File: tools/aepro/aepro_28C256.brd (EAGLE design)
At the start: 53 x 80 mm, 22 parts, among them IC1 MCP23017SP, IC2 MCP23008/P, U1 328P, Y1 16 MHz

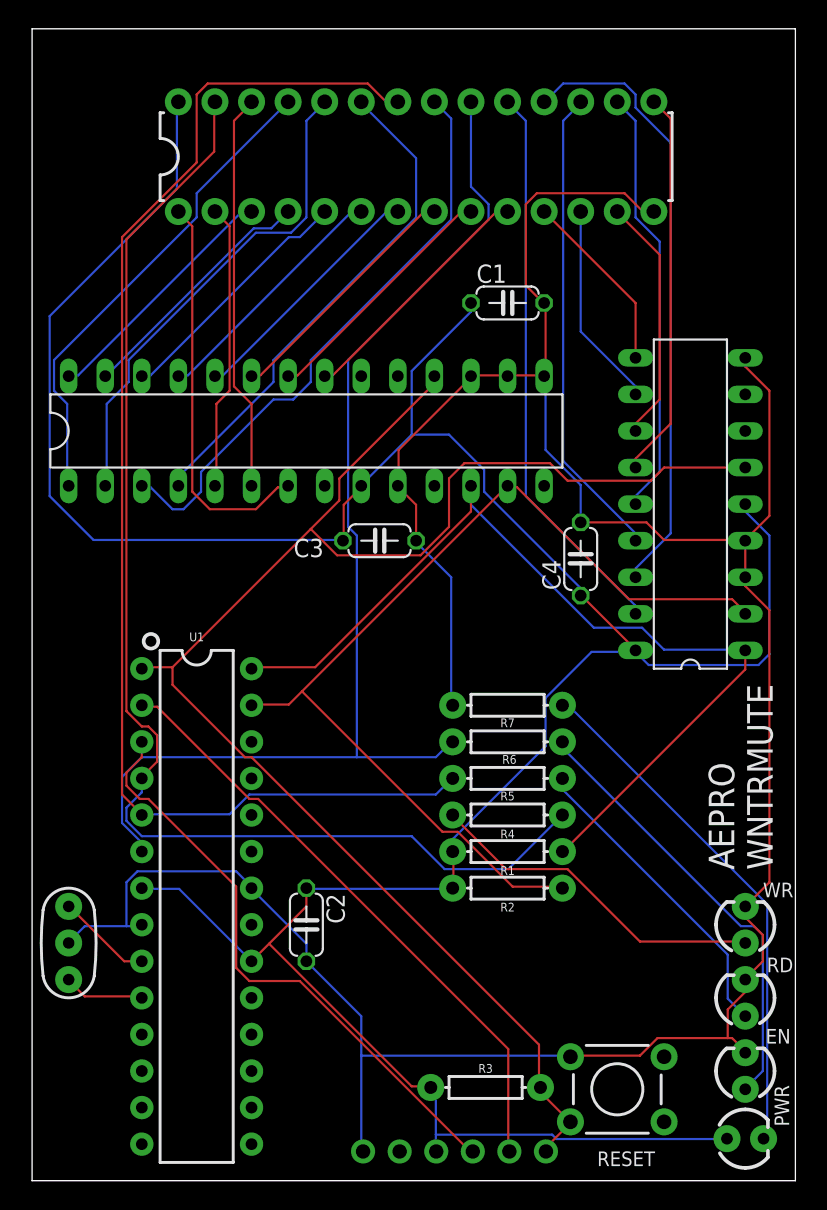
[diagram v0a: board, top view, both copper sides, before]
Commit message: Update several tool boards.
+ AEPRO had the wrong socket size; the ZIF footprint was for
  a narrow 28-pin DIP.
+ AEPRO was missing an inverter on the LEDs.
+ M328PGM had a serial line tied to RST: any attempt at using the
  UART caused the board to reset.
+ M1284PGM had no silkscreen markings to identify the board.
+ M1284PGM had no decoupling capacitor for the MCU.
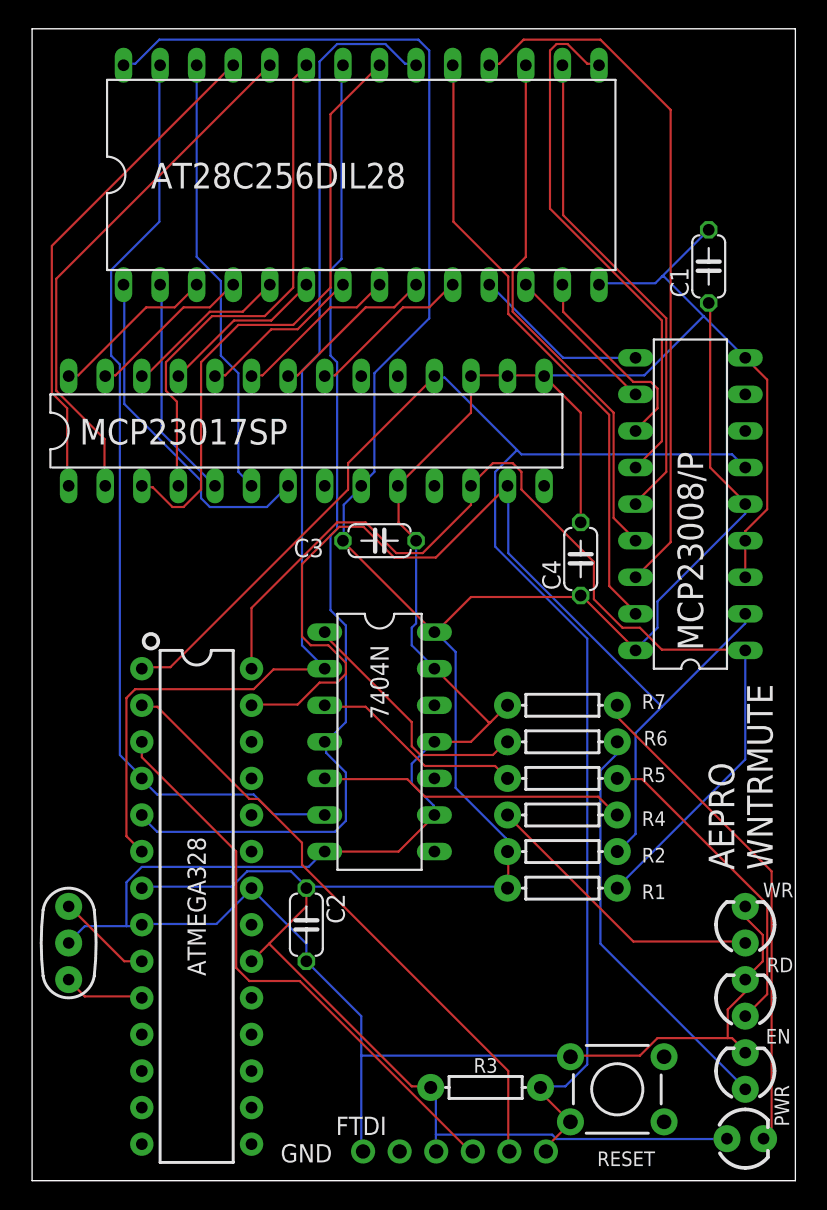
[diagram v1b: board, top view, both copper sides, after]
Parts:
- added V1: 7404N, 74ttl-din:DIL14
- R1, R2: value 4.7K -> (none)
- U$1: value AT28C256 -> AT28C256DIL28; device wntrmute:DIL28-3-ZIF_SOCKET -> wntrmute:DIL28-6
- moved C1 14.2 mm to (47.0, 63.5), turned to 90 degrees
- moved R1 4.58 mm to (36.8, 20.3)
- moved R2 4.58 mm to (36.8, 22.9)
- moved U$1 4.02 mm to (22.9, 69.8)
- moved R4 3.81 mm to (36.8, 25.4)
- moved R5 3.81 mm to (36.8, 27.9)
- moved R6 3.81 mm to (36.8, 30.5)
- moved R7 3.81 mm to (36.8, 33.0)
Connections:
- new net N$11: R5.P$1, V1.3
- new net N$15: R6.P$1, V1.1
- new net N$5: R4.P$1, V1.5
- net GND: now also V1.11, V1.13, V1.7, V1.9
- net N$2: now also V1.6; no longer R4.P$1
- net N$3: now also V1.4; no longer R5.P$1
- net N$4: now also V1.2; no longer R6.P$1
- net VCC: now also V1.14
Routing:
- net N$2: track 87.7 -> 65.6 mm
- net N$5: track 0.00 -> 21.4 mm
- net N$3: track 90.2 -> 69.9 mm
- net N$15: track 0.00 -> 17.8 mm
- net N$11: track 0.00 -> 14.8 mm
- net D3: track 26.9 -> 37.2 mm
- net GND: track 196.3 -> 205.4 mm
- net SCL: track 65.4 -> 73.1 mm
- net SDA: track 68.1 -> 75.4 mm
- net D6: track 42.7 -> 48.8 mm
- net A1: track 17.5 -> 11.6 mm
- net A7: track 17.5 -> 11.6 mm
- net A4: track 17.5 -> 11.6 mm
- net A2: track 17.5 -> 11.6 mm
- net A5: track 17.5 -> 11.6 mm
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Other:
- board text added: "ATMEGA328"
- board text added: "FTDI"
- board text added: "GND"
- board text added: "K_ISOM / OAK_CA REV6/20190930"
- board text removed: "K_ISOM / OAK_CA REV5/20190829"

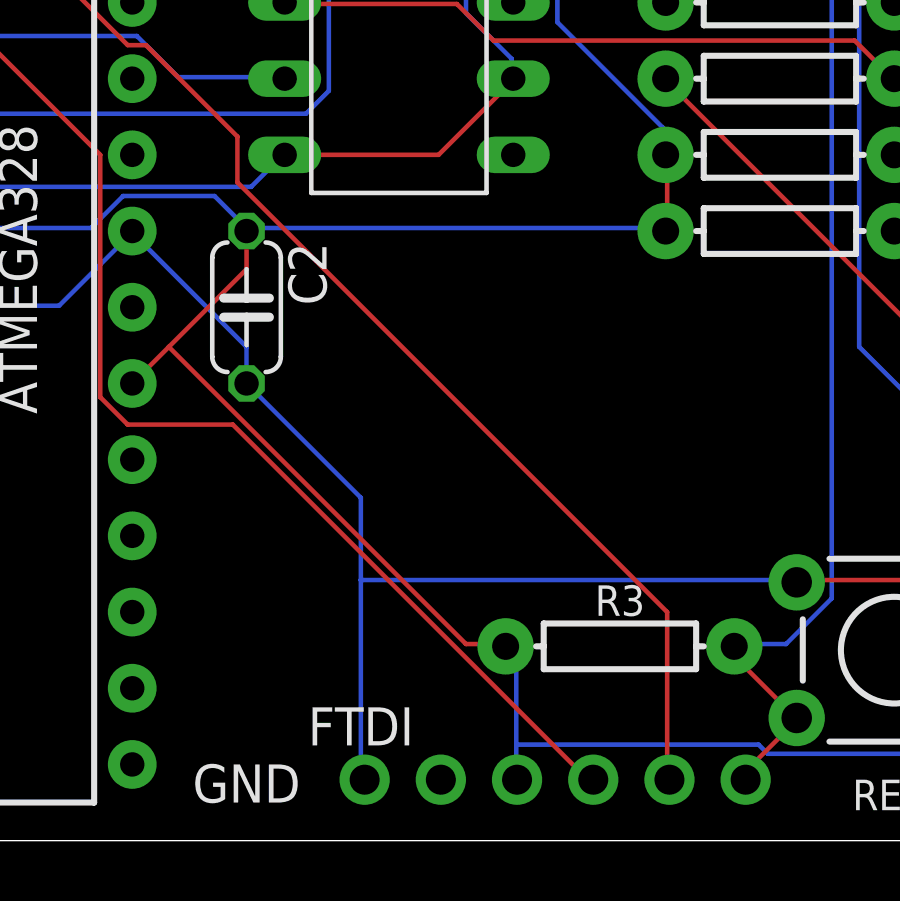
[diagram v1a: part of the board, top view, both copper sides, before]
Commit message: Fix UART lines on AEPRO.
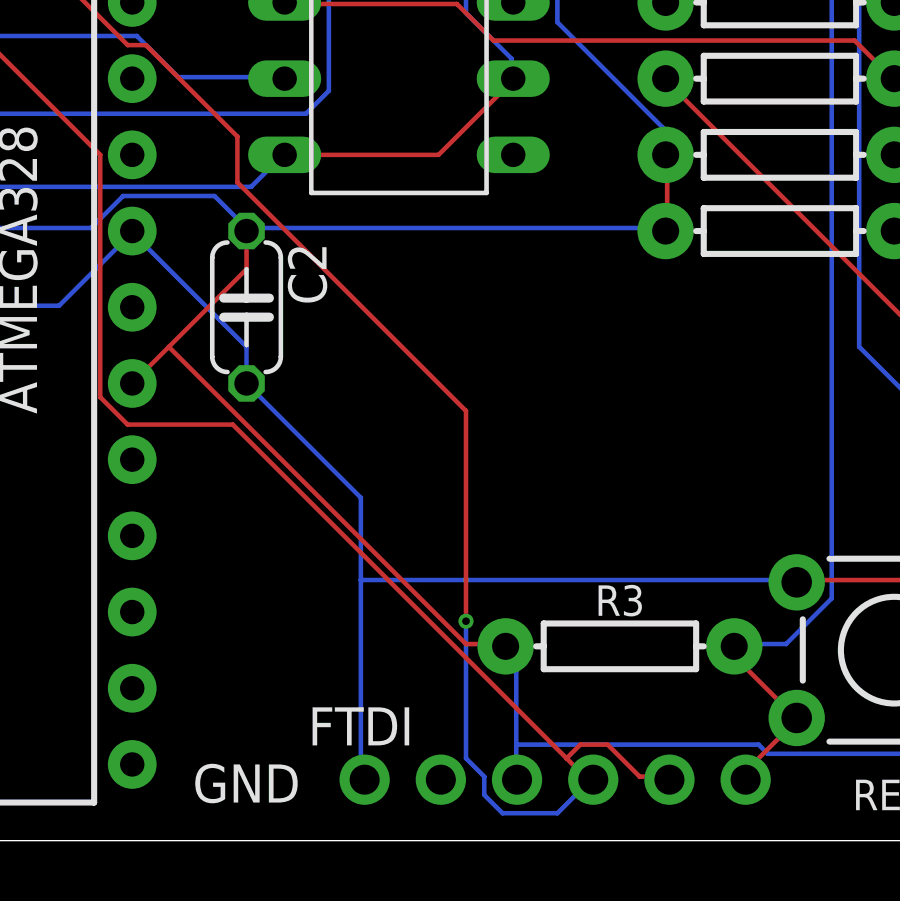
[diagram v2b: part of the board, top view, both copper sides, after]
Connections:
- net N$12: now also CN1.4; no longer CN1.5
- net N$6: now also CN1.5; no longer CN1.4
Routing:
- net N$6: track 40.2 -> 44.1 mm
- net N$12: track 42.5 -> 44.8 mm, vias 0 -> 1
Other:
- board text added: "K_ISOM / OAK_CA REV7/20191002"
- board text removed: "K_ISOM / OAK_CA REV6/20190930"
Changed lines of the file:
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@@
 <text x="39.243" y="2.032" size="1.016" layer="21" font="vector" align="top-left">RESET</text>
 <text x="49.53" y="76.2" size="1.016" layer="22" font="vector" rot="SMR270" align="top-left">K_ISOM / OAK_CA
-REV6/20190930</text>
+REV7/20191002</text>
 <text x="11.43" y="19.05" size="1.27" layer="21" rot="R90" align="center">ATMEGA328</text>
 <text x="22.86" y="3.81" size="1.27" layer="21" align="center">FTDI</text>
@@
 <signal name="N$6">
 <contactref element="U1" pad="3"/>
-<contactref element="CN1" pad="4"/>
 <wire x1="7.62" y1="29.4132" x2="7.62" y2="30.48" width="0.1524" layer="1"/>
 <wire x1="14.1732" y1="22.86" x2="7.62" y2="29.4132" width="0.1524" layer="1"/>
@@
 <wire x1="15.0876" y1="13.8684" x2="14.1732" y2="14.7828" width="0.1524" layer="1"/>
 <wire x1="18.5928" y1="13.8684" x2="15.0876" y2="13.8684" width="0.1524" layer="1"/>
-<wire x1="30.48" y1="1.9812" x2="18.5928" y2="13.8684" width="0.1524" layer="1"/>
-<wire x1="30.48" y1="1.9812" x2="30.607" y2="2.032" width="0.1524" layer="1"/>
+<wire x1="30.48" y1="1.9812" x2="29.718" y2="2.7432" width="0.1524" layer="1"/>
+<contactref element="CN1" pad="5"/>
+<wire x1="29.718" y1="2.7432" x2="18.5928" y2="13.8684" width="0.1524" layer="1"/>
+<wire x1="32.1564" y1="2.1336" x2="33.0708" y2="2.1336" width="0.1524" layer="1"/>
+<wire x1="31.0896" y1="3.2004" x2="32.1564" y2="2.1336" width="0.1524" layer="1"/>
+<wire x1="30.1752" y1="3.2004" x2="31.0896" y2="3.2004" width="0.1524" layer="1"/>
+<wire x1="29.718" y1="2.7432" x2="30.1752" y2="3.2004" width="0.1524" layer="1"/>
+<wire x1="33.0708" y1="2.1336" x2="33.147" y2="2.032" width="0.1524" layer="1"/>
 </signal>
 <signal name="N$7">
@@
 <wire x1="50.9016" y1="3.048" x2="50.8" y2="2.921" width="0.1524" layer="1"/>
 </signal>
-<signal name="N$12">
-<contactref element="CN1" pad="5"/>
-<contactref element="U1" pad="2"/>
-<wire x1="8.6868" y1="32.9184" x2="7.62" y2="32.9184" width="0.1524" layer="1"/>
-<wire x1="15.0876" y1="26.5176" x2="8.6868" y2="32.9184" width="0.1524" layer="1"/>
-<wire x1="15.6972" y1="26.5176" x2="15.0876" y2="26.5176" width="0.1524" layer="1"/>
-<wire x1="18.7452" y1="23.4696" x2="15.6972" y2="26.5176" width="0.1524" layer="1"/>
-<wire x1="18.7452" y1="21.9456" x2="18.7452" y2="23.4696" width="0.1524" layer="1"/>
-<wire x1="33.0708" y1="7.62" x2="18.7452" y2="21.9456" width="0.1524" layer="1"/>
-<wire x1="33.0708" y1="2.1336" x2="33.0708" y2="7.62" width="0.1524" layer="1"/>
-<wire x1="7.62" y1="32.9184" x2="7.62" y2="33.02" width="0.1524" layer="1"/>
-<wire x1="33.0708" y1="2.1336" x2="33.147" y2="2.032" width="0.1524" layer="1"/>
-</signal>
 <signal name="N$13">
 <contactref element="Y1" pad="1"/>
@@
 <wire x1="20.2692" y1="35.6616" x2="20.32" y2="35.56" width="0.1524" layer="16"/>
 </signal>
+<signal name="N$12">
+<contactref element="CN1" pad="4"/>
+<contactref element="U1" pad="2"/>
+<wire x1="8.6868" y1="32.9184" x2="7.62" y2="32.9184" width="0.1524" layer="1"/>
+<wire x1="15.0876" y1="26.5176" x2="8.6868" y2="32.9184" width="0.1524" layer="1"/>
+<wire x1="15.6972" y1="26.5176" x2="15.0876" y2="26.5176" width="0.1524" layer="1"/>
+<wire x1="18.7452" y1="23.4696" x2="15.6972" y2="26.5176" width="0.1524" layer="1"/>
+<wire x1="18.7452" y1="21.9456" x2="18.7452" y2="23.4696" width="0.1524" layer="1"/>
+<wire x1="26.3652" y1="14.3256" x2="18.7452" y2="21.9456" width="0.1524" layer="1"/>
+<wire x1="26.3652" y1="7.3152" x2="26.3652" y2="14.3256" width="0.1524" layer="1"/>
+<wire x1="26.3652" y1="2.7432" x2="26.3652" y2="7.3152" width="0.1524" layer="16"/>
+<wire x1="26.9748" y1="2.1336" x2="26.3652" y2="2.7432" width="0.1524" layer="16"/>
+<wire x1="26.9748" y1="1.524" x2="26.9748" y2="2.1336" width="0.1524" layer="16"/>
+<wire x1="27.5844" y1="0.9144" x2="26.9748" y2="1.524" width="0.1524" layer="16"/>
+<wire x1="29.4132" y1="0.9144" x2="27.5844" y2="0.9144" width="0.1524" layer="16"/>
+<wire x1="30.48" y1="1.9812" x2="29.4132" y2="0.9144" width="0.1524" layer="16"/>
+<wire x1="7.62" y1="32.9184" x2="7.62" y2="33.02" width="0.1524" layer="1"/>
+<wire x1="30.48" y1="1.9812" x2="30.607" y2="2.032" width="0.1524" layer="16"/>
+<via x="26.3652" y="7.3152" extent="1-16" drill="0.254"/>
+</signal>
 </signals>

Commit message: AEPRO rev 7
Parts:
- U$1: value AT28C256DIL28 -> AT28C256; device wntrmute:DIL28-6 -> wntrmute:DIL28-6-ZIF_SOCKET
- moved R7 21.6 mm to (26.7, 14.0)
- moved R6 17.3 mm to (26.7, 16.5)
- moved C2 17.1 mm to (2.92, 23.4)
- moved R1 15.3 mm to (26.7, 8.89), turned to 0 degrees
- moved R2 15.3 mm to (26.7, 11.4), turned to 0 degrees
- moved V1 14.5 mm to (38.1, 26.7)
- moved IC1 12.7 mm to (26.7, 41.9), turned to 270 degrees
- moved R5 12.0 mm to (26.7, 21.6)
- moved R4 12.0 mm to (26.7, 19.1), turned to 0 degrees
- moved C3 9.16 mm to (19.1, 36.8), turned to 270 degrees
- moved C4 8.03 mm to (45.7, 45.7), turned to 270 degrees
- moved IC2 7.73 mm to (38.1, 48.3), turned to 270 degrees
- moved D3 7.24 mm to (49.3, 19.9)
- moved C1 5.24 mm to (48.3, 58.4), turned to 0 degrees
- moved R3 4.83 mm to (26.7, 6.35)
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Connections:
- net N$2 renamed WE
- net N$3 renamed OE
- net N$4 renamed CE
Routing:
- net WE: track 65.6 -> 100.9 mm
- net SCL: track 73.1 -> 100.1 mm, vias 0 -> 1
- net OE: track 69.9 -> 92.6 mm
- net D6: track 48.8 -> 27.3 mm
- net N$7: track 110.0 -> 89.8 mm, vias 0 -> 1
- net D7: track 43.4 -> 27.0 mm
- net D0: track 12.3 -> 27.3 mm
- net A8: track 35.0 -> 21.7 mm
- net D1: track 10.9 -> 23.7 mm
- net CE: track 76.9 -> 89.4 mm, vias 0 -> 1
- net N$10: track 34.8 -> 22.6 mm
- net A3: track 11.5 -> 23.2 mm
- net A0: track 11.5 -> 23.2 mm
- net GND: track 205.4 -> 214.8 mm
- net A1: track 11.6 -> 20.8 mm
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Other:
- board text added: "10K"
- board text added: "330R"
- board text added: "4K7"
- board text added: "AEPRO/28"
- board text added: "AT28C256"
- board text added: "K_ISOM/OAK_CA"
- board text added: "OE: PD3 WE: PD2 CE: PD4 ADDR: $20 DATA: $21"
- board text added: "REV7/20191010"
- board text added: "RST"
- board text added: "RX"
- board text added: "STATUS"
- board text added: "TX"
- board text added: "WNTRMUTE"
- board text removed: "AEPRO WNTRMUTE"
- board text removed: "EN"
- board text removed: "K_ISOM / OAK_CA REV7/20191002"
- board text removed: "PWR"
- board text removed: "R1/R2: 4K7 R3: 10K ALL OTHER R: 330R C: 0.1µF"
- board text removed: "RD"
- board text removed: "RESET"
- board text removed: "WE: PD2 OE: PD3 CE: PD4 MCP23017: 0x20 MCP23008: 0x21"
- board text removed: "WR"
